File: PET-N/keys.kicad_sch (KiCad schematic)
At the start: 87 parts, among them J1 Extended_PET_keyboard_connect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, SW1 KP "=", SW10 KP "0", SW11 R SHIFT, SW12 ">", SW14 "]", SW15 "@", SW16 L SHIFT, SW17 KP "+", SW18 KP "2", SW2 KP ".", SW20 "?", SW21 ",", SW22 "N", SW23 "V", SW24 "X", SW25 KP "3", SW26 KP "1", SW27 RETURN, SW28 ";", SW29 "M", SW3 NC ($10), SW30 "B", SW31 "C", SW32 "Z", SW320 S LOCK, SW33 KP "*", SW34 KP "5", SW36 ":", SW37 "K", SW38 "H", SW39 "F", SW4 STOP, SW40 "S", SW41 KP "6", SW42 KP "4", SW44 "L", SW45 "J", SW46 "G", SW47 "D", SW48 "A", SW49 KP "/", SW5 "<", SW50 KP "8", SW52 "P", SW53 "I", SW54 "Y", SW55 "R", SW56 "W", SW57 KP "9", SW58 KP "7", SW59 U ARROW, SW6 SPACE, SW60 "O", SW61 "U", SW62 "T", SW63 "E", SW64 "Q", SW65 INS/DEL, SW66 UP/DOWN, SW67 NC ($0A), SW68 ")", SW69 "\", SW7 "[", SW70 "'", SW71 "$", SW72 QUOTE, SW73 LEFT/RIGHT, SW74 CLR/HOME, SW75 B ARROW, SW76 "(", SW77 "&", SW78 "%", SW79 "#", SW8 OFF/RVS, SW80 "!", SW9 KP "-"

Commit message: almost done routing; last checks still open
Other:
- note added: "(C) 2020,2021 Steve J. Gray (C) 2025 André Fachat"
- note added: "CBM-KEYB-PETN-3.0-20251005"
- note added: "CONNECTOR SWITCH"
- note added: "Joy Down"
- note added: "Joy Left"
- note added: "Joy Right"
- note added: "Joy Up"
- note added: "KEY CONFIGURATION JUMPERS"
- note added: "Locking MX switches are hard to get, but if you have one it can be used, or it can be jumpered for SW13 (new) or SW51 (sjg). Solder-jumper default is SW13. Cut/re-solder for other options."
- note added: "RELEASES: * N-V1-R1 PCB Submitted 2020-12-18 * N-V1-R2 PCB Updated 2021-03-31 * N-V3-R1 PCB Submitted 2025-10-05"
- note added: "Solder JP1 and JP2 if original 20 pin connector is used"
- note added: "This switch is not on the keyboard but is assigned PETSCII $0A in the matrix. We put it beside the SPACEBAR. We can change the function in firmware. Alternatively, you can assign it to the space key as well. Solder-jumper default is $0A. Cut/re-solder to map to SPACEBAR"
- note added: "This switch is not on the keyboard but is assigned the PETSCII $10 in the matrix. We put it beside the SPACEBAR. We can change the function in firmware. Alternatively, you can assign it to the space key as well. Solder-jumper default is $10. Cut/re-solder to map to SPACEBAR."
- note removed: "CONFIGURATION JUMPERS"
- note removed: "Locking MX switches are hard to get, but if you have one it can be used, or it can be jumpered for SW13 (new) or R51 (sjg)"
- note removed: "N-V1-R2"
- note removed: "RELEASES: * N-V1-R1 PCB Submitted 2020-12-18 * N-V1-R2 PCB Updated 2021-03-31"
- note removed: "This switch is not on the keyboard but is assigned PETSCII $0A in the matrix. We put it beside the SPACEBAR. We can change the function in firmware. Alternatively, you can assign it to the space key as well."
- note removed: "This switch is not on the keyboard but is assigned the PETSCII $10 in the matrix. We put it beside the SPACEBAR. We can change the function in firmware. Alternatively, you can assign it to the space key as well."
- moved on the sheet: JP1, JP10, JP11, JP2, JP3, JP4, JP6, JP7, JP8, JP9, SW320A, SW3A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

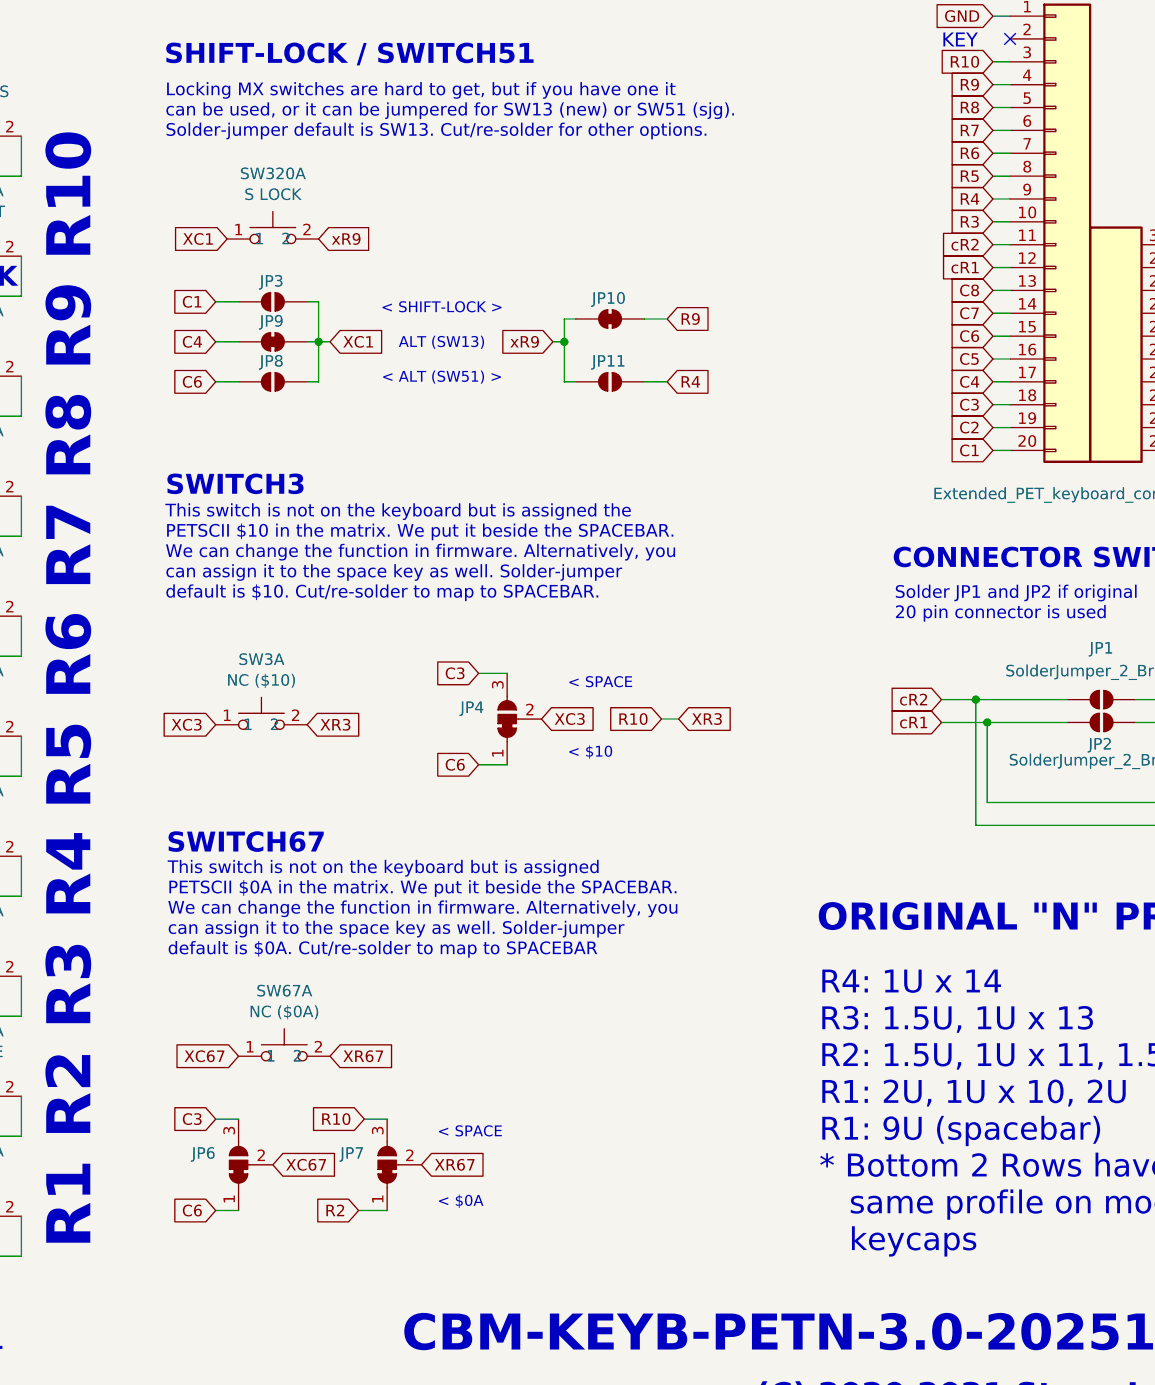
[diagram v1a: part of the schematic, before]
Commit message: fix Cn vs CCn bug, add proper joystick in schem; routing still to fix
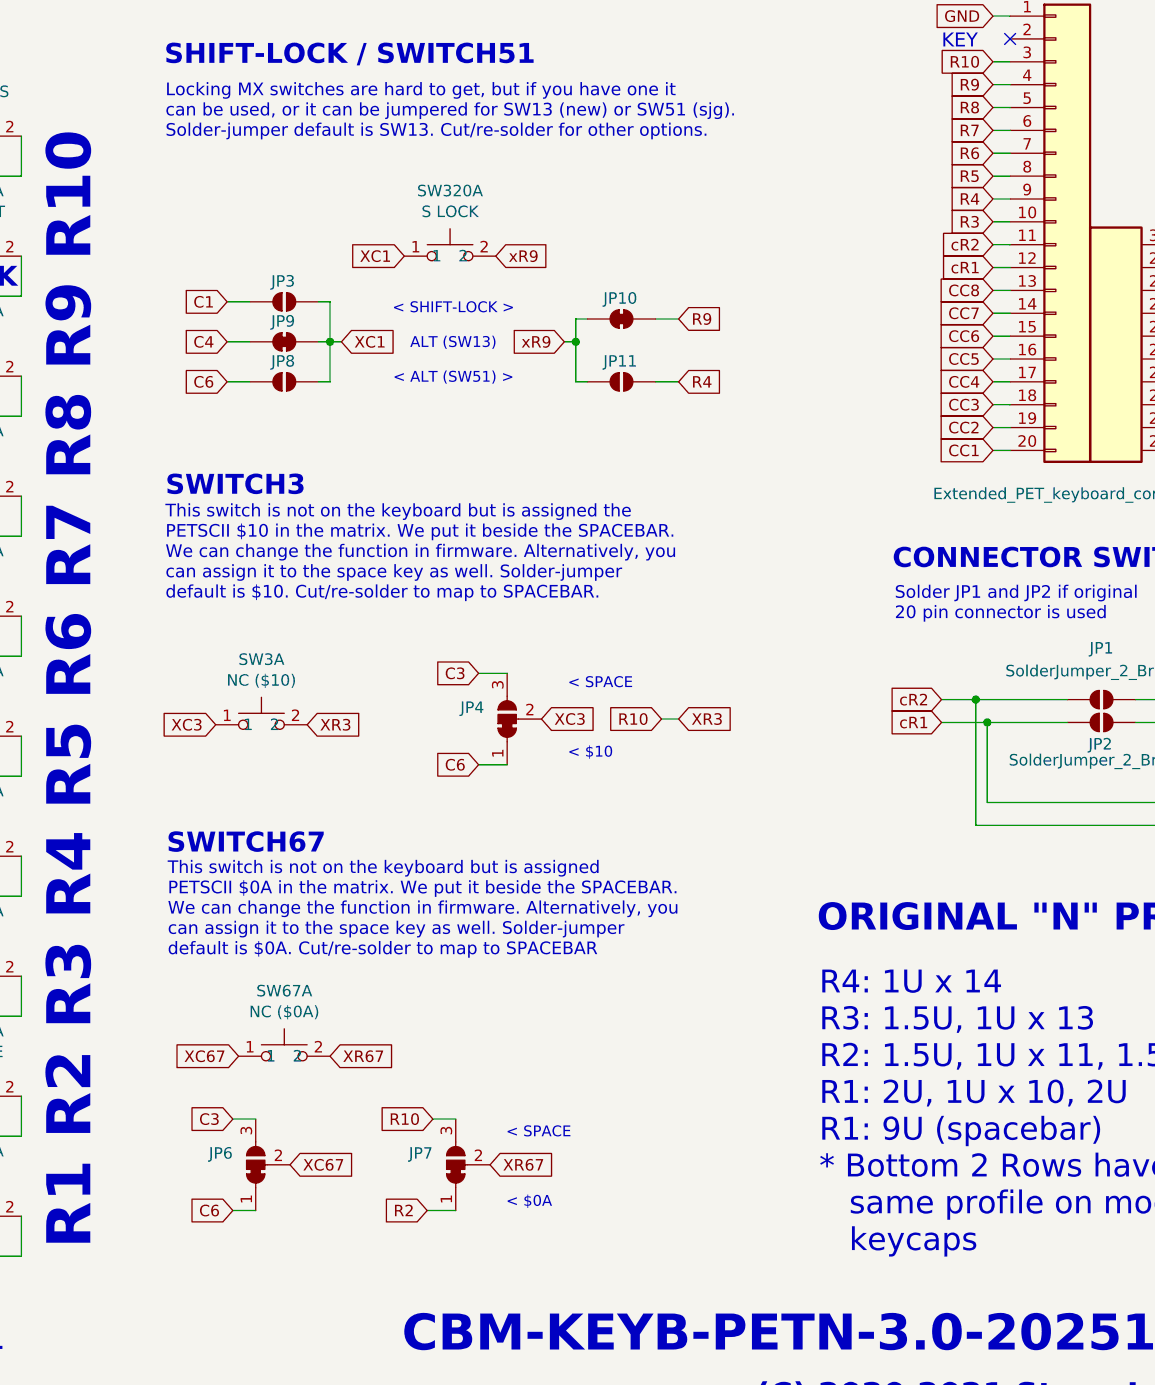
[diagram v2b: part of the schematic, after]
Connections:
- net C1: no longer J1.20 (C1)
- net C2: no longer J1.19 (C2)
- net C3: no longer J1.18 (C3)
- net C4: no longer J1.17 (C4)
- net C5: no longer J1.16 (C5)
- net C6: no longer J1.15 (C6)
- net C7: no longer J1.14 (C7)
- net C8: no longer J1.13 (C8)
- new net CC1: J1.20 (C1)
- new net CC2: J1.19 (C2)
- new net CC3: J1.18 (C3)
- new net CC4: J1.17 (C4)
- new net CC5: J1.16 (C5)
- new net CC6: J1.15 (C6)
- new net CC7: J1.14 (C7)
- new net CC8: J1.13 (C8)
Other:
- moved on the sheet: JP10, JP11, JP3, JP6, JP7, JP8, JP9, SW320A

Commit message: hopefully final schem and layout for 3.0A
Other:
- note added: "CBM-KEYB-PETN-3.0A-20251011"
- note added: "RELEASES: * N-V1-R1 PCB Submitted 2020-12-18 * N-V1-R2 PCB Updated 2021-03-31 * N-V3-R1 PCB Submitted 2025-10-11"
- note added: "Solder JP1 and JP2 if original 20 pin connector is used (i.e none of the controllers)"
- note removed: "CBM-KEYB-PETN-3.0-20251005"
- note removed: "RELEASES: * N-V1-R1 PCB Submitted 2020-12-18 * N-V1-R2 PCB Updated 2021-03-31 * N-V3-R1 PCB Submitted 2025-10-05"
- note removed: "Solder JP1 and JP2 if original 20 pin connector is used"
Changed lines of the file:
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@@
 		)
 	)
-	(text "RELEASES:\n* N-V1-R1 PCB Submitted 2020-12-18\n* N-V1-R2 PCB Updated 2021-03-31 \n* N-V3-R1 PCB Submitted 2025-10-05"
+	(text "RELEASES:\n* N-V1-R1 PCB Submitted 2020-12-18\n* N-V1-R2 PCB Updated 2021-03-31 \n* N-V3-R1 PCB Submitted 2025-10-11"
 		(exclude_from_sim no)
 		(at 100.838 193.04 0)
@@
 		)
 	)
-	(text "Solder JP1 and JP2 if original \n20 pin connector is used"
+	(text "Solder JP1 and JP2 if original \n20 pin connector is used (i.e\nnone of the controllers)"
 		(exclude_from_sim no)
 		(at 239.268 93.98 0)
@@
 		)
 	)
-	(text "CBM-KEYB-PETN-3.0-20251005"
+	(text "CBM-KEYB-PETN-3.0A-20251011"
 		(exclude_from_sim no)
 		(at 232.156 173.228 0)
@@
 	(text "CONNECTOR SWITCH"
 		(exclude_from_sim no)
-		(at 239.014 88.392 0)
-		(effects
-			(font
+		(at 238.76 86.614 0)
+		(effects
+			(font

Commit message: as sent to production
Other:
- note added: "CBM-KEYB-PETN-3.0A-20251014"
- note removed: "CBM-KEYB-PETN-3.0A-20251011"
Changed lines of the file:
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@@
 		)
 	)
-	(text "CBM-KEYB-PETN-3.0A-20251011"
+	(text "CBM-KEYB-PETN-3.0A-20251014"
 		(exclude_from_sim no)
 		(at 232.156 173.228 0)

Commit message: first run on r3.1
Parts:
- removed J1: Extended_PET_keyboard_connector, petkn:PET_Extended_Keyboard_Connector, symbol petkn:Extended_PET_keyboard_connector
- removed JP1, JP11, JP2, JP3, JP8: SolderJumper_2_Bridged, Jumper:SolderJumper-2_P1.3mm_Open_RoundedPad1.0x1.5mm, symbol Jumper:SolderJumper_2_Open
- removed JP10, JP9: SolderJumper_2_Bridged, Jumper:SolderJumper-2_P1.3mm_Bridged_RoundedPad1.0x1.5mm, symbol Jumper:SolderJumper_2_Bridged
- removed JP4, JP6, JP7: SolderJumper_3_Bridged12, Jumper:SolderJumper-3_P1.3mm_Bridged12_RoundedPad1.0x1.5mm_NumberLabels, symbol Jumper:SolderJumper_3_Bridged12
- removed SW3: NC ($10), petkn:SW_Cherry_MX_1.25u_PCB_with_RGB_LED, symbol petkn:MX Key with SMD RGB LED
- removed SW320: S LOCK, petkn:SW_Cherry_MX_1.50u_PCB_with_RGB_LED, symbol petkn:MX Key with SMD RGB LED
- removed SW67: NC ($0A), petkn:SW_Cherry_MX_1.50u_PCB_with_RGB_LED, symbol petkn:MX Key with SMD RGB LED
- added D10, D11, D12, D13, D14, D15, D16, D17, D18, D19, D2, D20, D21, D22, D23, D24, D25, D26, D27, D28, D29, D3, D30, D31, D32, D33, D34, D35, D36, D37, D38, D39, D4, D40, D41, D42, D43, D44, D45, D46, D47, D48, D49, D5, D50, D51, D52, D53, D54, D55, D56, D57, D58, D59, D6, D60, D61, D62, D63, D64, D65, D66, D67, D68, D69, D7, D70, D71, D72, D73, D74, D8, D9: 1N4448, Diode_SMD:D_SOD-323_HandSoldering, symbol PCM_Diode_AKL:1N4448
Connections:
- net R1: now also D11.1 (K), D21.1 (K), D31.1 (K), D41.1 (K), D50.1 (K), D60.1 (K), D64.1 (K), D74.1 (K); no longer SW73.2, SW74.2, SW75.2, SW76.2, SW77.2, SW78.2, SW79.2, SW80.2
- net R10: now also D12.1 (K), D2.1 (K), D22.1 (K), D32.1 (K), D33.1 (K), D51.1 (K), D65.1 (K); no longer SW1.2, SW2.2, SW4.2, SW5.2, SW6.2, SW7.2, SW8.2
- net R2: now also D20.1 (K), D30.1 (K), D40.1 (K), D49.1 (K), D6.1 (K), D63.1 (K), D73.1 (K); no longer SW65.2, SW66.2, SW68.2, SW69.2, SW70.2, SW71.2, SW72.2
- net R3: now also D10.1 (K), D19.1 (K), D29.1 (K), D39.1 (K), D48.1 (K), D58.1 (K), D62.1 (K), D72.1 (K); no longer SW57.2, SW58.2, SW59.2, SW60.2, SW61.2, SW62.2, SW63.2, SW64.2
- net R4: now also D18.1 (K), D28.1 (K), D38.1 (K), D47.1 (K), D5.1 (K), D61.1 (K), D71.1 (K); no longer SW49.2, SW50.2, SW52.2, SW53.2, SW54.2, SW55.2, SW56.2
- net R5: now also D17.1 (K), D27.1 (K), D37.1 (K), D46.1 (K), D59.1 (K), D70.1 (K), D9.1 (K); no longer SW41.2, SW42.2, SW44.2, SW45.2, SW46.2, SW47.2, SW48.2
- net R6: now also D16.1 (K), D26.1 (K), D36.1 (K), D4.1 (K), D45.1 (K), D57.1 (K), D69.1 (K); no longer SW33.2, SW34.2, SW36.2, SW37.2, SW38.2, SW39.2, SW40.2
- net R7: now also D15.1 (K), D25.1 (K), D35.1 (K), D44.1 (K), D54.1 (K), D56.1 (K), D68.1 (K), D8.1 (K); no longer SW25.2, SW26.2, SW27.2, SW28.2, SW29.2, SW30.2, SW31.2, SW32.2
- net R8: now also D14.1 (K), D24.1 (K), D3.1 (K), D34.1 (K), D43.1 (K), D55.1 (K), D67.1 (K); no longer SW17.2, SW18.2, SW20.2, SW21.2, SW22.2, SW23.2, SW24.2
- net R9: now also D13.1 (K), D23.1 (K), D42.1 (K), D52.1 (K), D53.1 (K), D66.1 (K), D7.1 (K); no longer SW10.2, SW11.2, SW12.2, SW14.2, SW15.2, SW16.2, SW9.2
- new net: D65.2 (A), SW1.2
- new net: D51.2 (A), SW2.2
- new net: D33.2 (A), SW4.2
- new net: D32.2 (A), SW5.2
- new net: D22.2 (A), SW6.2
- new net: D12.2 (A), SW7.2
- new net: D2.2 (A), SW8.2
- new net: D66.2 (A), SW9.2
- new net: D53.2 (A), SW10.2
- new net: D52.2 (A), SW11.2
- new net: D42.2 (A), SW12.2
- new net: D23.2 (A), SW14.2
- new net: D13.2 (A), SW15.2
- new net: D7.2 (A), SW16.2
- new net: D67.2 (A), SW17.2
- new net: D55.2 (A), SW18.2
- new net: D43.2 (A), SW20.2
- new net: D34.2 (A), SW21.2
- new net: D24.2 (A), SW22.2
- new net: D14.2 (A), SW23.2
- new net: D3.2 (A), SW24.2
- new net: D68.2 (A), SW25.2
- new net: D56.2 (A), SW26.2
- new net: D54.2 (A), SW27.2
- new net: D44.2 (A), SW28.2
- new net: D35.2 (A), SW29.2
- new net: D25.2 (A), SW30.2
- new net: D15.2 (A), SW31.2
- new net: D8.2 (A), SW32.2
- new net: D69.2 (A), SW33.2
- new net: D57.2 (A), SW34.2
- new net: D45.2 (A), SW36.2
- new net: D36.2 (A), SW37.2
- new net: D26.2 (A), SW38.2
- new net: D16.2 (A), SW39.2
- new net: D4.2 (A), SW40.2
- new net: D70.2 (A), SW41.2
- new net: D59.2 (A), SW42.2
- new net: D46.2 (A), SW44.2
- new net: D37.2 (A), SW45.2
- new net: D27.2 (A), SW46.2
- new net: D17.2 (A), SW47.2
- new net: D9.2 (A), SW48.2
- new net: D71.2 (A), SW49.2
- new net: D61.2 (A), SW50.2
- new net: D47.2 (A), SW52.2
- new net: D38.2 (A), SW53.2
- new net: D28.2 (A), SW54.2
- new net: D18.2 (A), SW55.2
- new net: D5.2 (A), SW56.2
- new net: D72.2 (A), SW57.2
- new net: D62.2 (A), SW58.2
- new net: D58.2 (A), SW59.2
- new net: D48.2 (A), SW60.2
- new net: D39.2 (A), SW61.2
- new net: D29.2 (A), SW62.2
- new net: D19.2 (A), SW63.2
- new net: D10.2 (A), SW64.2
- new net: D73.2 (A), SW65.2
- new net: D63.2 (A), SW66.2
- new net: D49.2 (A), SW68.2
- new net: D40.2 (A), SW69.2
- new net: D30.2 (A), SW70.2
- new net: D20.2 (A), SW71.2
- new net: D6.2 (A), SW72.2
- new net: D74.2 (A), SW73.2
- new net: D64.2 (A), SW74.2
- new net: D60.2 (A), SW75.2
- new net: D50.2 (A), SW76.2
- new net: D41.2 (A), SW77.2
- new net: D31.2 (A), SW78.2
- new net: D21.2 (A), SW79.2
- new net: D11.2 (A), SW80.2
- no-connect marks 1 -> 0
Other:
- note added: "(C) 2020, 2021 Steve J. Gray (C) 2025, 2026 André Fachat"
- note added: "CBM-KEYB-PETN-3.1A-20260130"
- note removed: "(C) 2020,2021 Steve J. Gray (C) 2025 André Fachat"
- note removed: "< SHIFT-LOCK > ALT (SW13) < ALT (SW51) >"
- note removed: "< SPACE < $0A"
- note removed: "< SPACE < $10"
- note removed: "CBM-KEYB-PETN-3.0A-20251014"
- note removed: "CONNECTOR SWITCH"
- note removed: "CONNECTORS"
- note removed: "KEY"
- note removed: "KEY CONFIGURATION JUMPERS"
- note removed: "Locking MX switches are hard to get, but if you have one it can be used, or it can be jumpered for SW13 (new) or SW51 (sjg). Solder-jumper default is SW13. Cut/re-solder for other options."
- note removed: "ORIGINAL "N" PROFILE"
- note removed: "PET/CBM "N" KEYBOARD"
- note removed: "R4: 1U x 14 R3: 1.5U, 1U x 13 R2: 1.5U, 1U x 11, 1.5U R1: 2U, 1U x 10, 2U R1: 9U (spacebar) * Bottom 2 Rows have same profile on modern keycaps"
- note removed: "RELEASES: * N-V1-R1 PCB Submitted 2020-12-18 * N-V1-R2 PCB Updated 2021-03-31 * N-V3-R1 PCB Submitted 2025-10-11"
- note removed: "SHIFT-LOCK / SWITCH51"
- note removed: "SWITCH3"
- note removed: "SWITCH67"
- note removed: "Solder JP1 and JP2 if original 20 pin connector is used (i.e none of the controllers)"
- note removed: "Standard "N" layout with the following changes: - SPACEBAR now 6.25U. Two keys added beside it. - SHIFTLOCK is configurable - Jumpers to make extra keys work as SPACEBAR or Alternate"
- note removed: "This switch is not on the keyboard but is assigned PETSCII $0A in the matrix. We put it beside the SPACEBAR. We can change the function in firmware. Alternatively, you can assign it to the space key as well. Solder-jumper default is $0A. Cut/re-solder to map to SPACEBAR"
- note removed: "This switch is not on the keyboard but is assigned the PETSCII $10 in the matrix. We put it beside the SPACEBAR. We can change the function in firmware. Alternatively, you can assign it to the space key as well. Solder-jumper default is $10. Cut/re-solder to map to SPACEBAR."
- moved on the sheet: SW10A, SW11A, SW12A, SW14A, SW15A, SW16A, SW17A, SW18A, SW1A, SW20A, SW21A, SW22A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

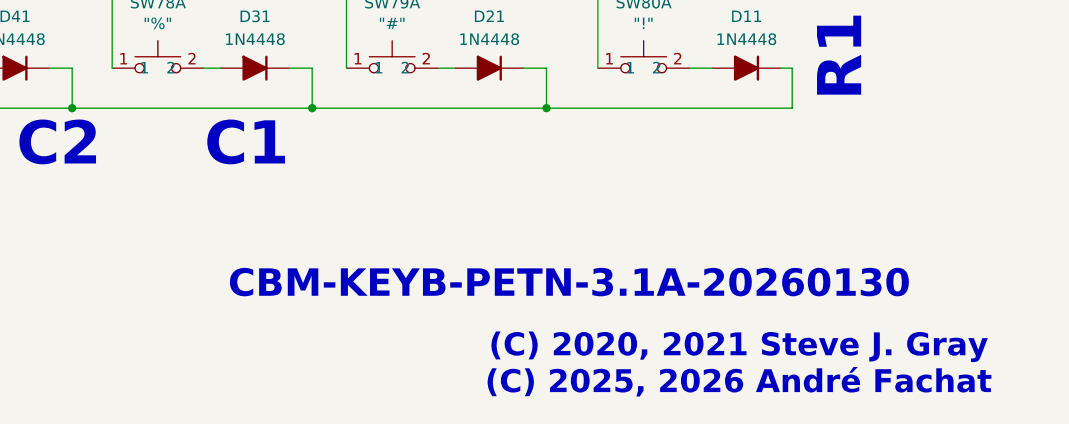
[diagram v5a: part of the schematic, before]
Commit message: add orientation marker for backlight LEDs and move to 3.1B
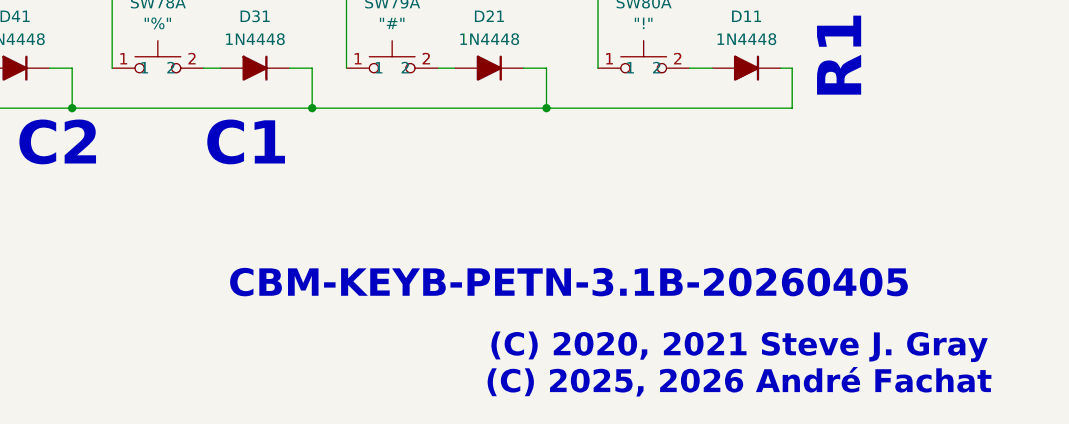
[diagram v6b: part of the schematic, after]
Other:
- note added: "CBM-KEYB-PETN-3.1B-20260405"
- note removed: "CBM-KEYB-PETN-3.1A-20260130"
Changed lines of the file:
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@@
 		)
 	)
-	(text "CBM-KEYB-PETN-3.1A-20260130"
+	(text "CBM-KEYB-PETN-3.1B-20260405"
 		(exclude_from_sim no)
 		(at 228.6 175.895 0)
